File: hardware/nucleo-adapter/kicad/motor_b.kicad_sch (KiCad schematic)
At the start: 33 parts, among them J6 Motor B phase U, J7 Motor B phase V, J8 Motor B phase W, Q10 CSD16327Q3, Q11 CSD16327Q3, Q12 CSD16327Q3, Q13 CSD16327Q3, Q8 CSD16327Q3, Q9 CSD16327Q3, U6 DRV8300D (B), U7 INA180A2

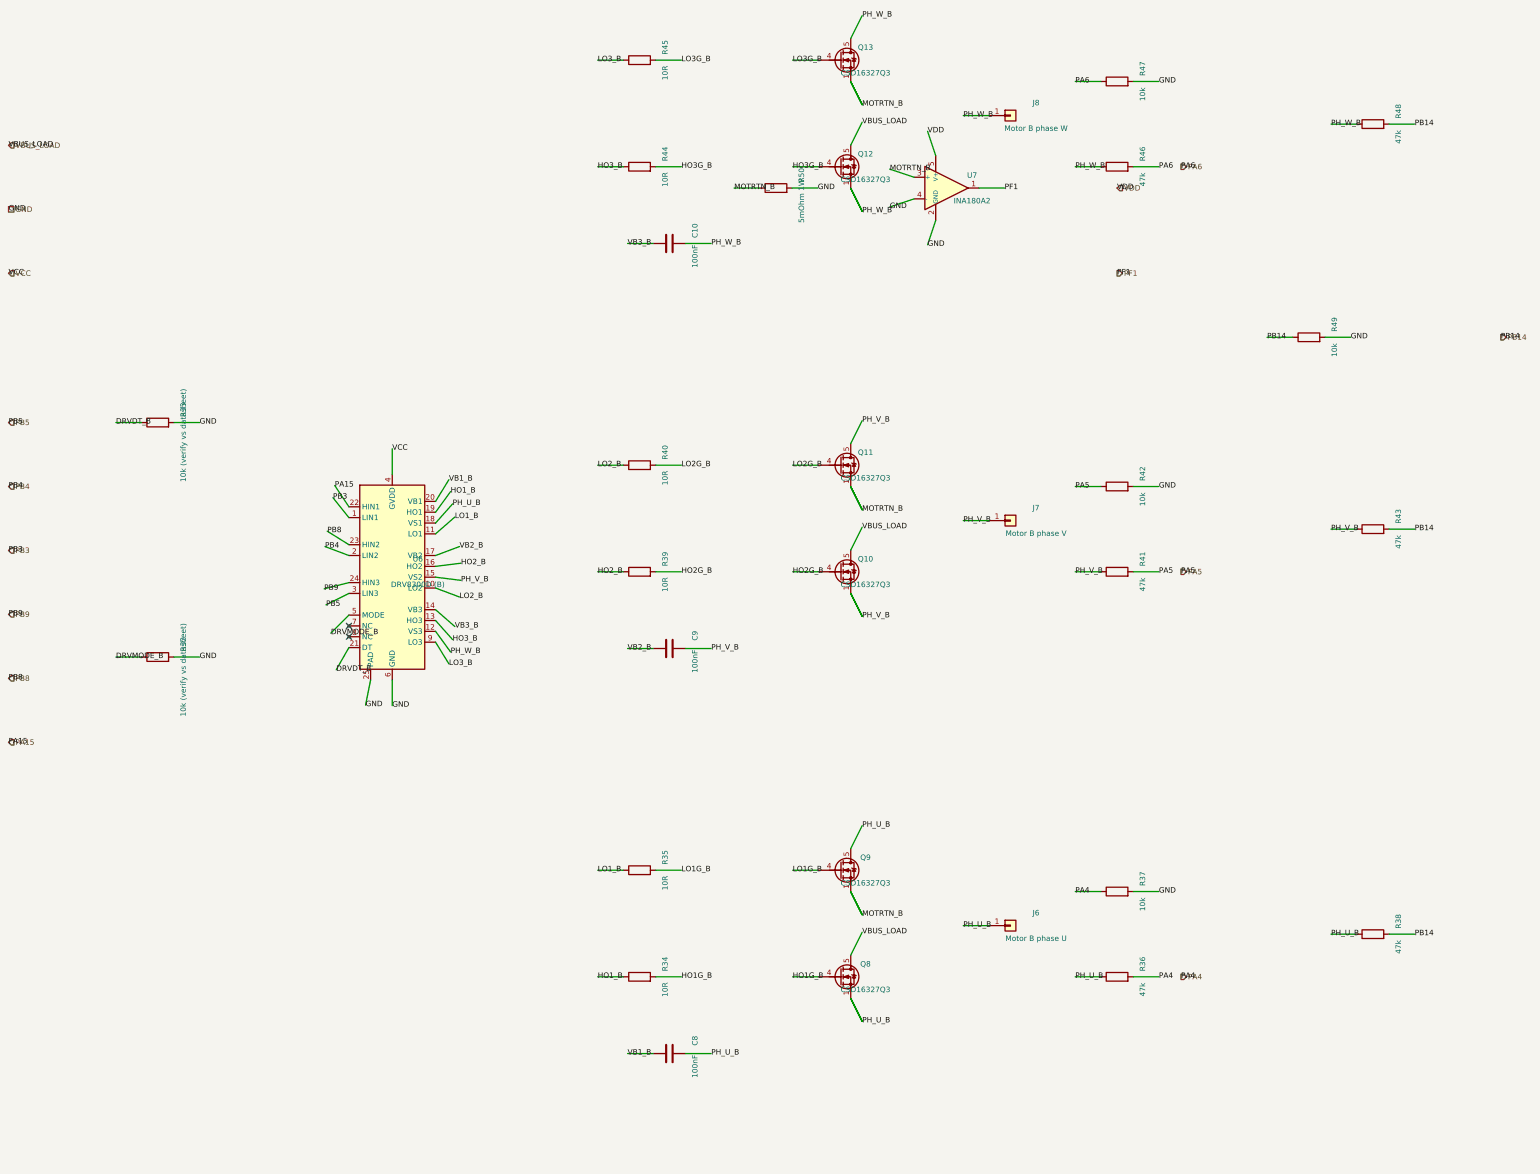
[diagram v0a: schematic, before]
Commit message: Place real Nucleo-G474RE symbol and fold it into the project libraries
Replaces the hand-authored black-box Nucleo block with the genuine
STMicroelectronics/SnapEDA symbol, wired by real CN7/CN10 pin number
rather than guessed pin names, and routed through dedicated lanes since
the real pinout doesn't line up with the sheets' pin order the way the
old placeholder did.

The symbol and its footprint were previously loose, unregistered files
(the footprint's library nickname didn't even exist in fp-lib-table).
Both now live inside the project's registered AdapterSymbols.kicad_sym
and AdapterFootprints.pretty libraries, referenced accordingly.

Co-Authored-By: Claude Sonnet 5 <noreply@anthropic.com>
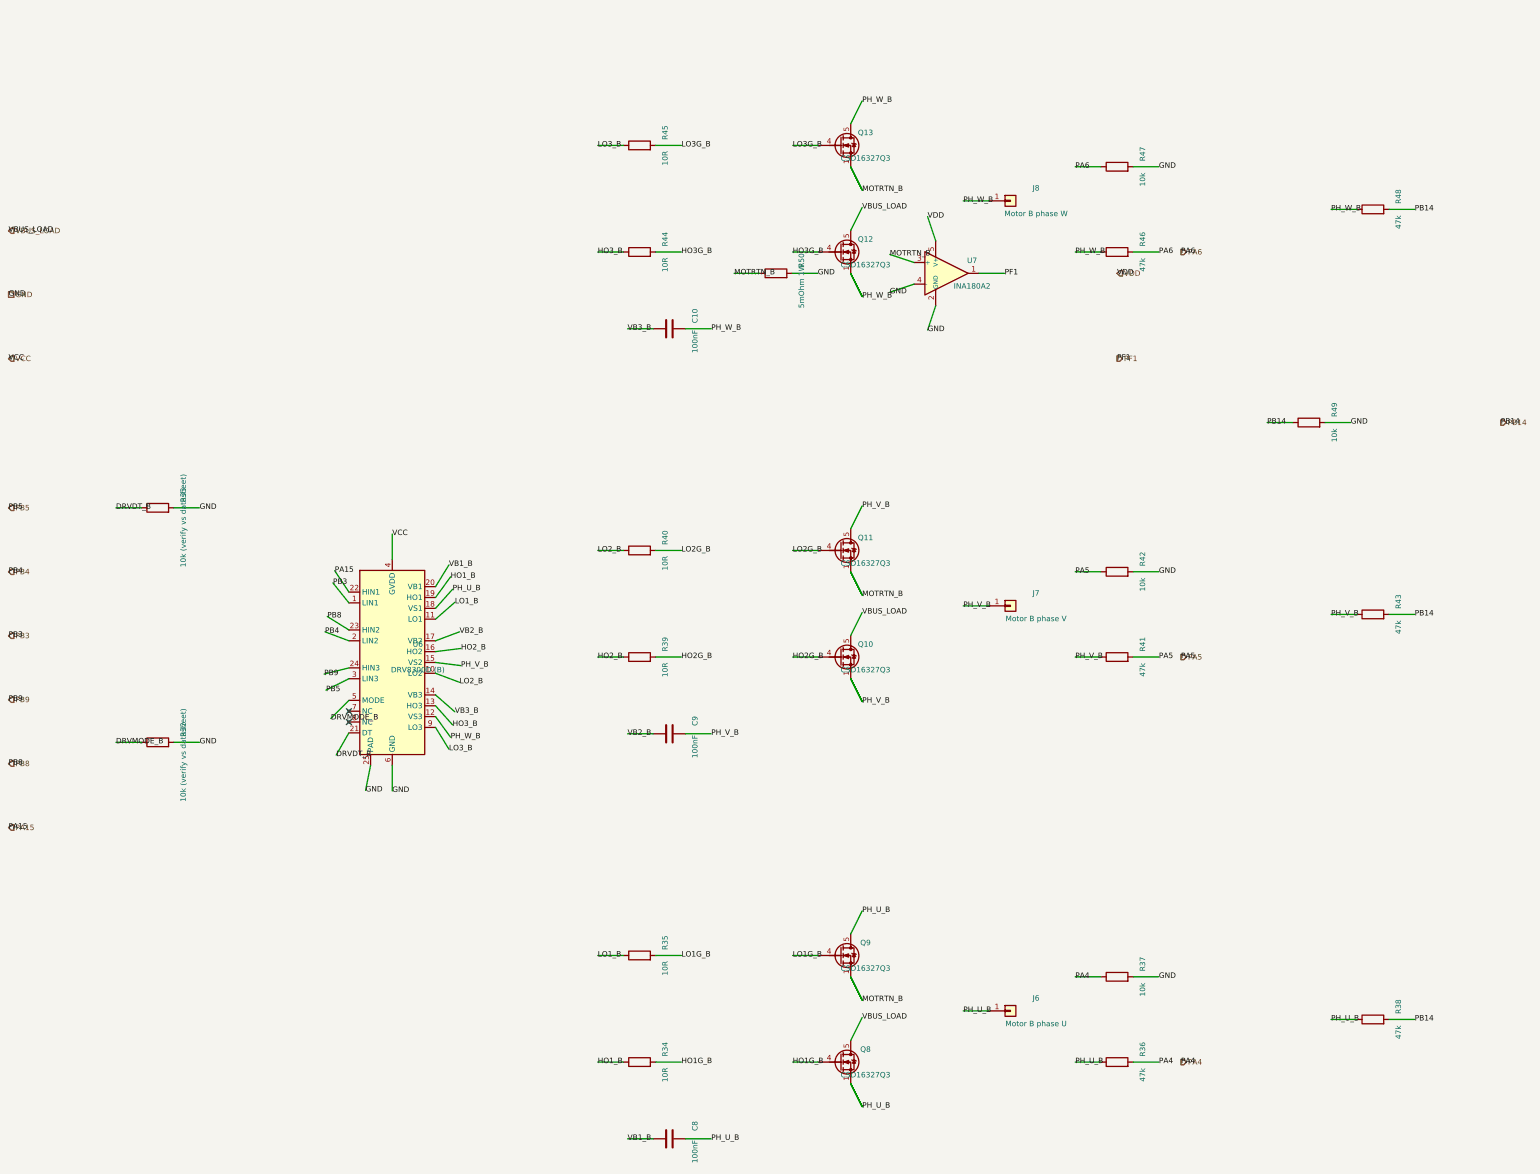
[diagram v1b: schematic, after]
